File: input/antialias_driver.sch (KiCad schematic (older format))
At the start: 20 parts, among them U104 THS4131

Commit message: Cleanup to get ready to start board layout. I had to get rid off all the bus signals, since in Kicad busses don't work that way.  Added a couple testpoints; many more needed.
Work on component placement in PCB.  I changed DGND to plain GND and "protective earth" to
"earth" (for chassis ground).  Chassis ground is now connected on the board only via a capacitor.
I had to fix the connector footprint to match the pin numbers on the symbol (there was a case
difference).
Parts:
- D109, D110: symbol Diode:BAV99 -> ilemt_input:BAS21S
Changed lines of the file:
@@
 	3450 4100 3550 4100
 $Comp
-L Diode:BAV99 D?
-U 2 1 5E3F98E8
+L ilemt_input:BAS21S D?
+U 1 1 5E3F98E8
 P 7000 2900
 AR Path="/5DFCF14D/5DE42731/5E3F98E8" Ref="D?"  Part="2"
-AR Path="/5DFCF14D/5DE6CDF8/5E3F98E8" Ref="D109"  Part="2"
+AR Path="/5DFCF14D/5DE6CDF8/5E3F98E8" Ref="D109"  Part="1"
 F 0 "D109" H 7000 3115 50  0000 C CNN
 F 1 "BAS21S" H 7000 3024 50  0000 C CNN
 F 2 "Package_TO_SOT_SMD:SOT-23" H 7000 2750 50  0001 C CNN
 F 3 "https://assets.nexperia.com/documents/data-sheet/BAV99_SER.pdf" H 7000 3000 50  0001 C CNN
-	2    7000 2900
+	1    7000 2900
 	0    1    1    0
 $EndComp
 $Comp
-L Diode:BAV99 D?
-U 1 1 5E3F98EE
+L ilemt_input:BAS21S D?
+U 2 1 5E3F98EE
 P 7000 2400
 AR Path="/5DFCF14D/5DE42731/5E3F98EE" Ref="D?"  Part="1"
-AR Path="/5DFCF14D/5DE6CDF8/5E3F98EE" Ref="D109"  Part="1"
+AR Path="/5DFCF14D/5DE6CDF8/5E3F98EE" Ref="D109"  Part="2"
 F 0 "D109" H 7000 2615 50  0000 C CNN
 F 1 "BAS21S" H 7000 2524 50  0000 C CNN
 F 2 "Package_TO_SOT_SMD:SOT-23" H 7000 2250 50  0001 C CNN
 F 3 "https://assets.nexperia.com/documents/data-sheet/BAV99_SER.pdf" H 7000 2500 50  0001 C CNN
-	1    7000 2400
+	2    7000 2400
 	0    1    1    0
 $EndComp
@@
 	7000 2200 7000 2250
 $Comp
-L Diode:BAV99 D?
-U 2 1 5E403D60
+L ilemt_input:BAS21S D?
+U 1 1 5E403D60
 P 7000 4400
 AR Path="/5DFCF14D/5DE42731/5E403D60" Ref="D?"  Part="2"
-AR Path="/5DFCF14D/5DE6CDF8/5E403D60" Ref="D110"  Part="2"
+AR Path="/5DFCF14D/5DE6CDF8/5E403D60" Ref="D110"  Part="1"
 F 0 "D110" H 7000 4615 50  0000 C CNN
 F 1 "BAS21S" H 7000 4524 50  0000 C CNN
 F 2 "Package_TO_SOT_SMD:SOT-23" H 7000 4250 50  0001 C CNN
 F 3 "https://assets.nexperia.com/documents/data-sheet/BAV99_SER.pdf" H 7000 4500 50  0001 C CNN
-	2    7000 4400
+	1    7000 4400
 	0    1    1    0
 $EndComp
 $Comp
-L Diode:BAV99 D?
-U 1 1 5E403D66
+L ilemt_input:BAS21S D?
+U 2 1 5E403D66
 P 7000 3900
 AR Path="/5DFCF14D/5DE42731/5E403D66" Ref="D?"  Part="1"
-AR Path="/5DFCF14D/5DE6CDF8/5E403D66" Ref="D110"  Part="1"
+AR Path="/5DFCF14D/5DE6CDF8/5E403D66" Ref="D110"  Part="2"
 F 0 "D110" H 7000 4115 50  0000 C CNN
 F 1 "BAS21S" H 7000 4024 50  0000 C CNN
 F 2 "Package_TO_SOT_SMD:SOT-23" H 7000 3750 50  0001 C CNN
 F 3 "https://assets.nexperia.com/documents/data-sheet/BAV99_SER.pdf" H 7000 4000 50  0001 C CNN
-	1    7000 3900
+	2    7000 3900
 	0    1    1    0
 $EndComp

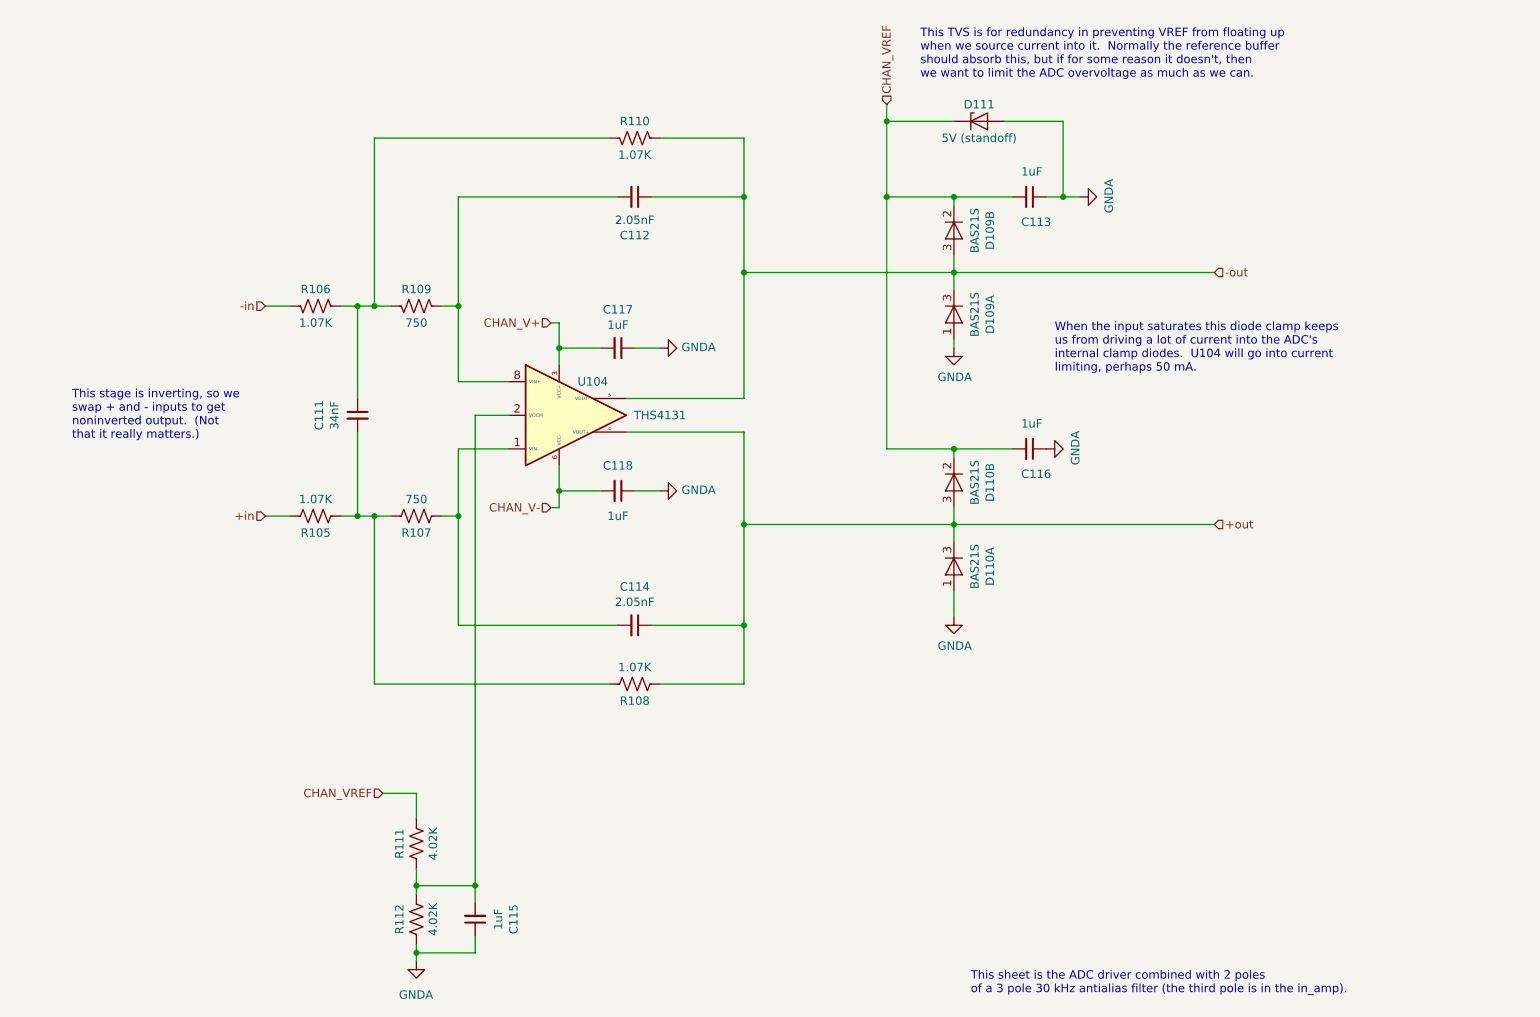
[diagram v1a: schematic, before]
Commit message: Changed board connector to PCIe 8x, added test points, cleanup of component values. Add LVDS Rx termination, bypass caps.
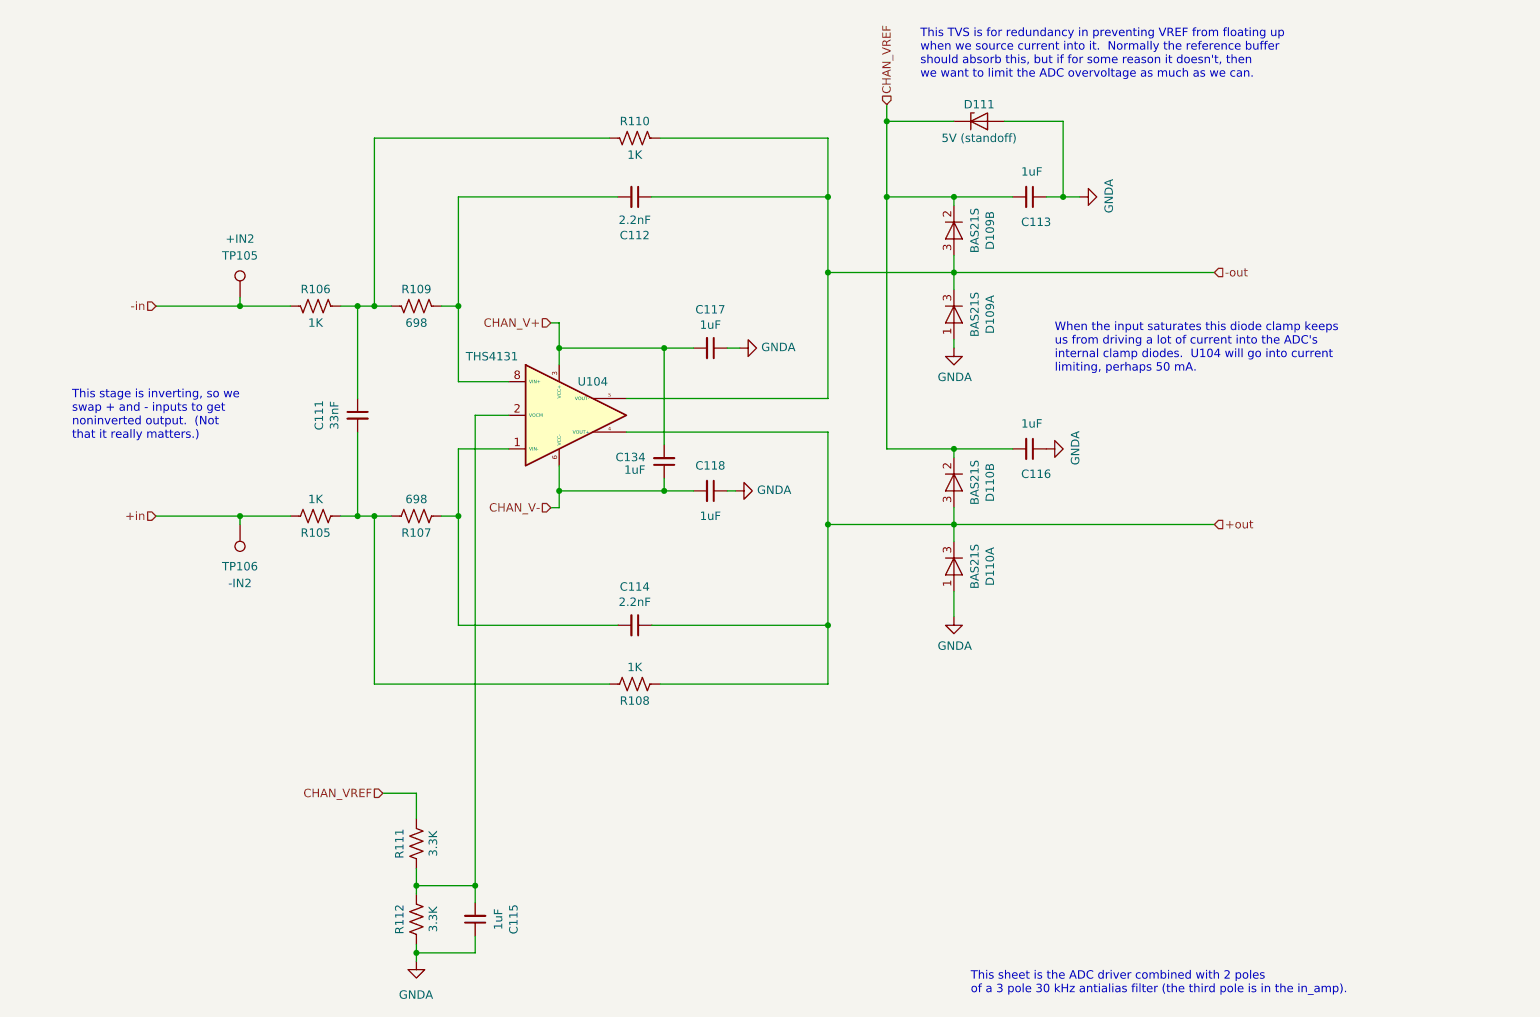
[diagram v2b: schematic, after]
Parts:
- added C134: 1uF, Capacitor_SMD:C_0805_2012Metric, symbol Device:C_Small
- added TP105: +IN2, TestPoint:TestPoint_THTPad_D1.5mm_Drill0.7mm, symbol Connector:TestPoint
- added TP106: -IN2, TestPoint:TestPoint_THTPad_D1.5mm_Drill0.7mm, symbol Connector:TestPoint
- C111: value 34nF -> 33nF; footprint Capacitor_SMD:C_0603_1608Metric -> Capacitor_SMD:C_0805_2012Metric; Description (none) -> CAP CER 0.033UF 50V C0G 0805; Digikey (none) -> 445-6950-1-ND
- C112, C114: value 2.05nF -> 2.2nF; footprint Capacitor_SMD:C_0603_1608Metric -> Capacitor_SMD:C_0805_2012Metric; Notes (none) -> 2% C0G
- R105, R106, R108, R110: value 1.07K -> 1K; Notes (none) -> 0.1%
- R107, R109: value 750 -> 698; Notes (none) -> 0.1%
- R111, R112: value 4.02K -> 3.3K; footprint Resistor_SMD:R_0805_2012Metric -> Resistor_SMD:R_0603_1608Metric
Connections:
- net +in: now also TP106.1
- net -in: now also TP105.1
- net CHAN_V+: now also C134.2
- net CHAN_V-: now also C134.1
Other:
- moved on the sheet: C117, C118

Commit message: Checkpoint before starting routing.  Added power and ground testpoints.
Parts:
- C111: DK line (none) -> 37; Description CAP CER 0.033UF 50V C0G 0805 -> 0.033µF ±5% 50V Ceramic Capacitor C0G, NP0 0805 (2012 Metri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
- C112, C114: footprint Capacitor_SMD:C_0805_2012Metric -> Capacitor_SMD:C_0603_1608Metric; DK line (none) -> 36; Description (none) -> 2200pF ±2% 50V Ceramic Capacitor C0G, NP0 0603 (1608 Metric); Digikey (none) -> 490-6381-1-ND
- C113, C115, C116, C117, C118, C134: DK line (none) -> 27
- D109, D110: DK line (none) -> 43; Description (none) -> DIODE ARRAY GP 250V 225MA SOT23; Digikey (none) -> BAS21SLT1GOSCT-ND; MPN (none) -> BAS21SLT1G
- D111: DK line (none) -> 40
- R105, R106, R108, R110: DK line (none) -> 48; Description (none) -> RES SMD 1K OHM 0.1% 1/10W 0603; Digikey (none) -> P1.0KDBCT-ND
- R107, R109: DK line (none) -> 47; Description (none) -> 698 Ohms ±0.5% 0.1W, 1/10W Chip Resistor 0603 (1608 Metric)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; Digikey (none) -> 311-2653-1-ND
- R111, R112: DK line (none) -> 53; Description (none) -> 3.3 kOhms ±1% 0.1W, 1/10W Chip Resistor 0603 (1608 Metric) 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; Digikey (none) -> YAG3354CT-ND; Notes 0.1% -> (none)
- U104: DK line (none) -> 42; Description (none) -> IC OPAMP DIFF 1 CIRCUIT 8SOIC; Digikey (none) -> 296-46339-1-ND
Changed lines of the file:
@@
 EESchema Schematic File Version 4
-LIBS:input_board-cache
-EELAYER 29 0
+EELAYER 30 0
 EELAYER END
 $Descr A4 11693 8268
@@
 F 5 "1276-6471-1-ND" H 5550 3100 50  0001 C CNN "Digikey"
 F 6 "CL21B105KOFNNNG" H 5550 3100 50  0001 C CNN "MPN"
+F 7 "27" H 5550 3100 50  0001 C CNN "DK line"
 	1    5550 3100
 	0    1    1    0
@@
 F 1 "698" V 3700 4100 50  0000 C CNN
 F 2 "Resistor_SMD:R_0603_1608Metric" V 3840 4090 50  0001 C CNN
-F 3 "~" H 3800 4100 50  0001 C CNN
+F 3 "" H 3800 4100 50  0001 C CNN
 F 4 "0.1%" H 3800 4100 50  0001 C CNN "Notes"
+F 5 "47" H 3800 4100 50  0001 C CNN "DK line"
+F 6 "698 Ohms ±0.5% 0.1W, 1/10W Chip Resistor 0603 (1608 Metric)  Thin Film" H 3800 4100 50  0001 C CNN "Description"
+F 7 "311-2653-1-ND" H 3800 4100 50  0001 C CNN "Digikey"
 	1    3800 4100
 	0    1    1    0
@@
 F 3 "~" H 5100 5100 50  0001 C CNN
 F 4 "0.1%" H 5100 5100 50  0001 C CNN "Notes"
+F 5 "48" H 5100 5100 50  0001 C CNN "DK line"
+F 6 "RES SMD 1K OHM 0.1% 1/10W 0603" H 5100 5100 50  0001 C CNN "Description"
+F 7 "P1.0KDBCT-ND" H 5100 5100 50  0001 C CNN "Digikey"
 	1    5100 5100
 	0    1    1    0
@@
 F 0 "C114" V 4871 4750 50  0000 C CNN
 F 1 "2.2nF" V 4962 4750 50  0000 C CNN
-F 2 "Capacitor_SMD:C_0805_2012Metric" H 5100 4750 50  0001 C CNN
-F 3 "~" H 5100 4750 50  0001 C CNN
+F 2 "Capacitor_SMD:C_0603_1608Metric" H 5100 4750 50  0001 C CNN
+F 3 "https://www.murata.com/~/media/webrenewal/support/library/catalog/products/capacitor/mlcc/c02e.ashx?la=en-us" H 5100 4750 50  0001 C CNN
 F 4 "2% C0G" H 5100 4750 50  0001 C CNN "Notes"
+F 5 "36" H 5100 4750 50  0001 C CNN "DK line"
+F 6 "2200pF ±2% 50V Ceramic Capacitor C0G, NP0 0603 (1608 Metric)" H 5100 4750 50  0001 C CNN "Description"
+F 7 "490-6381-1-ND" H 5100 4750 50  0001 C CNN "Digikey"
 	1    5100 4750
 	0    1    1    0
@@
 F 1 "33nF" V 3312 3500 50  0000 C CNN
 F 2 "Capacitor_SMD:C_0805_2012Metric" H 3450 3500 50  0001 C CNN
-F 3 "~" H 3450 3500 50  0001 C CNN
-F 4 "CAP CER 0.033UF 50V C0G 0805" H 3450 3500 50  0001 C CNN "Description"
+F 3 "https://product.tdk.com/info/en/documents/chara_sheet/CGA4J2C0G1H333J125AA.pdf?ref_disty=digikey" H 3450 3500 50  0001 C CNN
+F 4 "0.033µF ±5% 50V Ceramic Capacitor C0G, NP0 0805 (2012 Metric)" H 3450 3500 50  0001 C CNN "Description"
 F 5 "445-6950-1-ND" H 3450 3500 50  0001 C CNN "Digikey"
+F 6 "37" H 3450 3500 50  0001 C CNN "DK line"
 	1    3450 3500
 	1    0    0    -1
@@
 F 3 "~" H 3200 4100 50  0001 C CNN
 F 4 "0.1%" H 3200 4100 50  0001 C CNN "Notes"
+F 5 "48" H 3200 4100 50  0001 C CNN "DK line"
+F 6 "RES SMD 1K OHM 0.1% 1/10W 0603" H 3200 4100 50  0001 C CNN "Description"
+F 7 "P1.0KDBCT-ND" H 3200 4100 50  0001 C CNN "Digikey"
 	1    3200 4100
 	0    1    1    0
@@
 F 1 "THS4131" H 4250 3850 50  0000 C CNN
 F 2 "Package_SO:SO-8_5.3x6.2mm_P1.27mm" H 4650 3100 50  0001 C CNN
-F 3 "https://www.analog.com/media/en/technical-documentation/data-sheets/ADA4940-1_4940-2.pdf" H 2950 4700 50  0001 C CNN
+F 3 "http://www.ti.com/general/docs/suppproductinfo.tsp?distId=10&gotoUrl=http%3A%2F%2Fwww.ti.com%2Flit%2Fgpn%2Fths4131" H 2950 4700 50  0001 C CNN
+F 4 "42" H 4650 3500 50  0001 C CNN "DK line"
+F 5 "IC OPAMP DIFF 1 CIRCUIT 8SOIC" H 4650 3500 50  0001 C CNN "Description"
+F 6 "296-46339-1-ND" H 4650 3500 50  0001 C CNN "Digikey"
 	1    4650 3500
 	1    0    0    -1
@@
 F 2 "Resistor_SMD:R_0603_1608Metric" V 3840 6040 50  0001 C CNN
 F 3 "~" H 3800 6050 50  0001 C CNN
-F 4 "0.1%" H 3800 6050 50  0001 C CNN "Notes"
+F 4 "" H 3800 6050 50  0001 C CNN "Notes"
+F 5 "53" H 3800 6050 50  0001 C CNN "DK line"
+F 6 "3.3 kOhms ±1% 0.1W, 1/10W Chip Resistor 0603 (1608 Metric)  Thin Film" H 3800 6050 50  0001 C CNN "Description"
+F 7 "YAG3354CT-ND" H 3800 6050 50  0001 C CNN "Digikey"
 	1    3800 6050
 	-1   0    0    1
@@
 F 2 "Resistor_SMD:R_0603_1608Metric" V 3840 6490 50  0001 C CNN
 F 3 "~" H 3800 6500 50  0001 C CNN
-F 4 "0.1%" H 3800 6500 50  0001 C CNN "Notes"
+F 4 "" H 3800 6500 50  0001 C CNN "Notes"
+F 5 "53" H 3800 6500 50  0001 C CNN "DK line"
+F 6 "3.3 kOhms ±1% 0.1W, 1/10W Chip Resistor 0603 (1608 Metric)  Thin Film" H 3800 6500 50  0001 C CNN "Description"
+F 7 "YAG3354CT-ND" H 3800 6500 50  0001 C CNN "Digikey"
 	1    3800 6500
 	-1   0    0    1
@@
 F 5 "1276-6471-1-ND" H 4150 6500 50  0001 C CNN "Digikey"
 F 6 "CL21B105KOFNNNG" H 4150 6500 50  0001 C CNN "MPN"
+F 7 "27" H 4150 6500 50  0001 C CNN "DK line"
 	1    4150 6500
 	-1   0    0    1
@@
 F 5 "1276-6471-1-ND" H 5550 3950 50  0001 C CNN "Digikey"
 F 6 "CL21B105KOFNNNG" H 5550 3950 50  0001 C CNN "MPN"
+F 7 "27" H 5550 3950 50  0001 C CNN "DK line"
 	1    5550 3950
 	0    1    1    0
@@
 F 1 "698" V 3700 2850 50  0000 C CNN
 F 2 "Resistor_SMD:R_0603_1608Metric" V 3840 2840 50  0001 C CNN
-F 3 "~" H 3800 2850 50  0001 C CNN
+F 3 "" H 3800 2850 50  0001 C CNN
 F 4 "0.1%" H 3800 2850 50  0001 C CNN "Notes"
+F 5 "47" H 3800 2850 50  0001 C CNN "DK line"
+F 6 "698 Ohms ±0.5% 0.1W, 1/10W Chip Resistor 0603 (1608 Metric)  Thin Film" H 3800 2850 50  0001 C CNN "Description"
+F 7 "311-2653-1-ND" H 3800 2850 50  0001 C CNN "Digikey"
 	1    3800 2850
 	0    1    -1   0
@@
 F 3 "~" H 5100 1850 50  0001 C CNN
 F 4 "0.1%" H 5100 1850 50  0001 C CNN "Notes"
+F 5 "48" H 5100 1850 50  0001 C CNN "DK line"
+F 6 "RES SMD 1K OHM 0.1% 1/10W 0603" H 5100 1850 50  0001 C CNN "Description"
+F 7 "P1.0KDBCT-ND" H 5100 1850 50  0001 C CNN "Digikey"
 	1    5100 1850
 	0    1    -1   0
@@
 F 0 "C112" V 4871 2200 50  0000 C CNN
 F 1 "2.2nF" V 4962 2200 50  0000 C CNN
-F 2 "Capacitor_SMD:C_0805_2012Metric" H 5100 2200 50  0001 C CNN
-F 3 "~" H 5100 2200 50  0001 C CNN
+F 2 "Capacitor_SMD:C_0603_1608Metric" H 5100 2200 50  0001 C CNN
+F 3 "https://www.murata.com/~/media/webrenewal/support/library/catalog/products/capacitor/mlcc/c02e.ashx?la=en-us" H 5100 2200 50  0001 C CNN
 F 4 "2% C0G" H 5100 2200 50  0001 C CNN "Notes"
+F 5 "36" H 5100 2200 50  0001 C CNN "DK line"
+F 6 "2200pF ±2% 50V Ceramic Capacitor C0G, NP0 0603 (1608 Metric)" H 5100 2200 50  0001 C CNN "Description"
+F 7 "490-6381-1-ND" H 5100 2200 50  0001 C CNN "Digikey"
 	1    5100 2200
 	0    1    -1   0
@@
 F 3 "~" H 3200 2850 50  0001 C CNN
 F 4 "0.1%" H 3200 2850 50  0001 C CNN "Notes"
+F 5 "48" H 3200 2850 50  0001 C CNN "DK line"
+F 6 "RES SMD 1K OHM 0.1% 1/10W 0603" H 3200 2850 50  0001 C CNN "Description"
+F 7 "P1.0KDBCT-ND" H 3200 2850 50  0001 C CNN "Digikey"
 	1    3200 2850
 	0    1    -1   0
@@
 F 2 "Package_TO_SOT_SMD:SOT-23" H 7000 2750 50  0001 C CNN
 F 3 "https://assets.nexperia.com/documents/data-sheet/BAV99_SER.pdf" H 7000 3000 50  0001 C CNN
+F 4 "43" H 7000 2900 50  0001 C CNN "DK line"
+F 5 "DIODE ARRAY GP 250V 225MA SOT23" H 7000 2900 50  0001 C CNN "Description"
+F 6 "BAS21SLT1GOSCT-ND" H 7000 2900 50  0001 C CNN "Digikey"
+F 7 "BAS21SLT1G" H 7000 2900 50  0001 C CNN "MPN"
 	1    7000 2900
 	0    1    1    0
@@
 F 2 "Package_TO_SOT_SMD:SOT-23" H 7000 2250 50  0001 C CNN
 F 3 "https://assets.nexperia.com/documents/data-sheet/BAV99_SER.pdf" H 7000 2500 50  0001 C CNN
+F 4 "43" H 7000 2400 50  0001 C CNN "DK line"
+F 5 "DIODE ARRAY GP 250V 225MA SOT23" H 7000 2400 50  0001 C CNN "Description"
+F 6 "BAS21SLT1GOSCT-ND" H 7000 2400 50  0001 C CNN "Digikey"
+F 7 "BAS21SLT1G" H 7000 2400 50  0001 C CNN "MPN"
 	2    7000 2400
 	0    1    1    0
@@
 F 5 "1276-6471-1-ND" H 7450 2200 50  0001 C CNN "Digikey"
 F 6 "CL21B105KOFNNNG" H 7450 2200 50  0001 C CNN "MPN"
+F 7 "27" H 7450 2200 50  0001 C CNN "DK line"
 	1    7450 2200
 	0    1    1    0
@@
 F 2 "Package_TO_SOT_SMD:SOT-23" H 7000 4250 50  0001 C CNN
 F 3 "https://assets.nexperia.com/documents/data-sheet/BAV99_SER.pdf" H 7000 4500 50  0001 C CNN
+F 4 "43" H 7000 4400 50  0001 C CNN "DK line"
+F 5 "DIODE ARRAY GP 250V 225MA SOT23" H 7000 4400 50  0001 C CNN "Description"
+F 6 "BAS21SLT1GOSCT-ND" H 7000 4400 50  0001 C CNN "Digikey"
+F 7 "BAS21SLT1G" H 7000 4400 50  0001 C CNN "MPN"
 	1    7000 4400
 	0    1    1    0
@@
 F 2 "Package_TO_SOT_SMD:SOT-23" H 7000 3750 50  0001 C CNN
 F 3 "https://assets.nexperia.com/documents/data-sheet/BAV99_SER.pdf" H 7000 4000 50  0001 C CNN
+F 4 "43" H 7000 3900 50  0001 C CNN "DK line"
+F 5 "DIODE ARRAY GP 250V 225MA SOT23" H 7000 3900 50  0001 C CNN "Description"
+F 6 "BAS21SLT1GOSCT-ND" H 7000 3900 50  0001 C CNN "Digikey"
+F 7 "BAS21SLT1G" H 7000 3900 50  0001 C CNN "MPN"
 	2    7000 3900
 	0    1    1    0
@@
 F 5 "1276-6471-1-ND" H 7450 3700 50  0001 C CNN "Digikey"
 F 6 "CL21B105KOFNNNG" H 7450 3700 50  0001 C CNN "MPN"
+F 7 "27" H 7450 3700 50  0001 C CNN "DK line"
 	1    7450 3700
 	0    1    1    0
@@
 F 5 "TVS DIODE 5V 9.2V DO214AC" H 7150 1750 50  0001 C CNN "Description"
 F 6 "732-9974-1-ND" H 7150 1750 50  0001 C CNN "Digikey"
+F 7 "40" H 7150 1750 50  0001 C CNN "DK line"
 	1    7150 1750
 	1    0    0    -1
@@
 F 5 "1276-6471-1-ND" H 5275 3775 50  0001 C CNN "Digikey"
 F 6 "CL21B105KOFNNNG" H 5275 3775 50  0001 C CNN "MPN"
+F 7 "27" H 5275 3775 50  0001 C CNN "DK line"
 	1    5275 3775
 	-1   0    0    1
